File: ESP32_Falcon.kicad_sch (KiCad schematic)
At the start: 12 parts, among them J1 USB_C_Receptacle_USB2.0_16P, Q1 UMH3N, U1 ESP32-S3-WROOM-1, U2 USBLC6-2SC6, U3 AMS1117-3.3

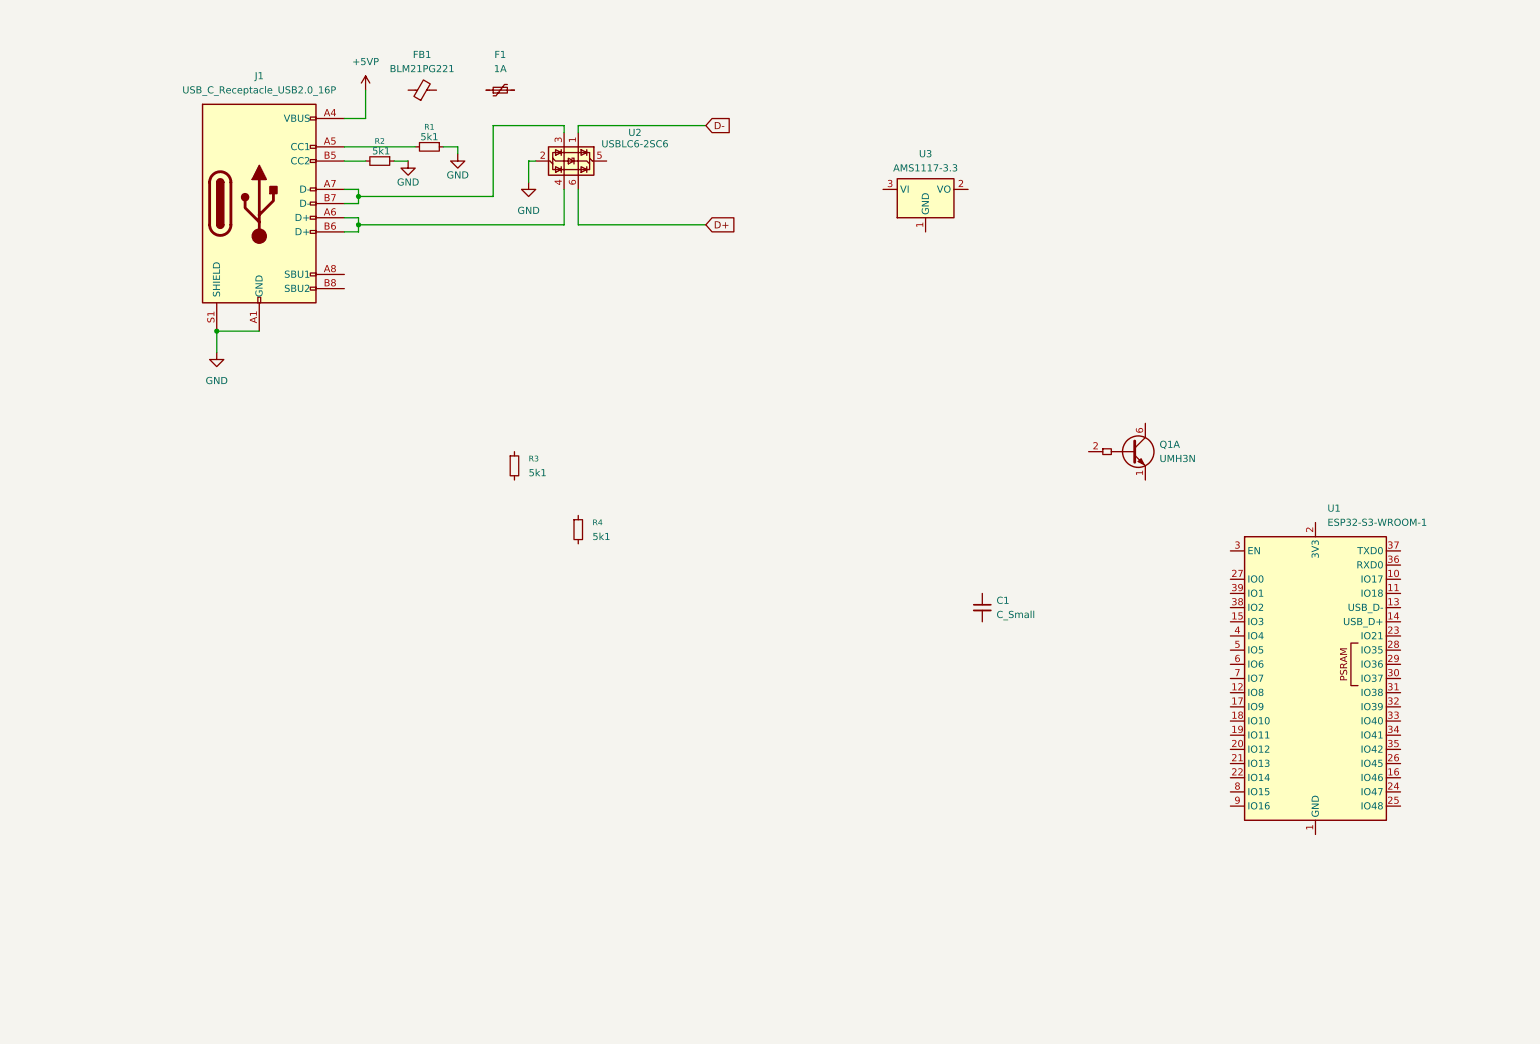
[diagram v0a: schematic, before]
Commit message: Praktycznie skonczony schematic
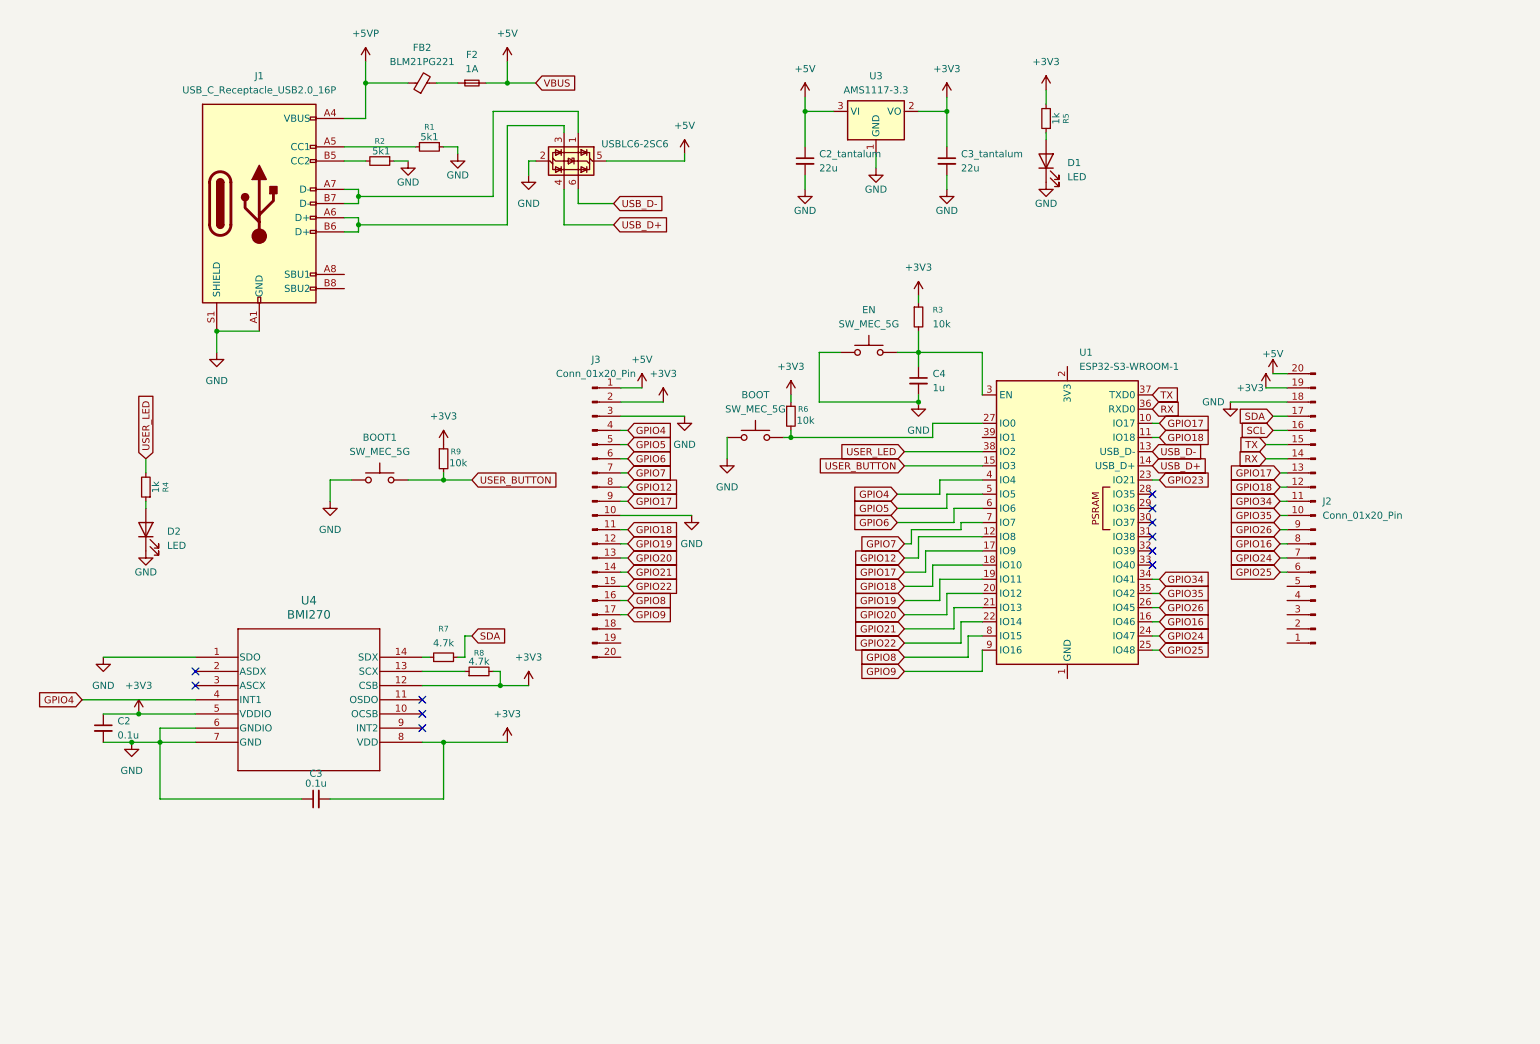
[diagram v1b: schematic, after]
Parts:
- removed C1: C_Small, Capacitor_SMD:C_0805_2012Metric_Pad1.18x1.45mm_HandSolder, symbol Device:C_Small
- removed F1: 1A, symbol Device:Polyfuse_Small
- removed FB1: BLM21PG221, symbol Device:FerriteBead_Small
- removed Q1: UMH3N, Package_TO_SOT_SMD:SOT-363_SC-70-6, symbol Transistor_BJT:UMH3N
- added BOOT, BOOT1: SW_MEC_5G, symbol Switch:SW_MEC_5G
- added C2, C3: 0.1u, Capacitor_SMD:C_0805_2012Metric_Pad1.18x1.45mm_HandSolder, symbol Device:C_Small
- added C2_tantalum, C3_tantalum: 22u, Capacitor_SMD:C_0805_2012Metric_Pad1.18x1.45mm_HandSolder, symbol Device:C_Small
- added C4: 1u, Capacitor_SMD:C_0805_2012Metric_Pad1.18x1.45mm_HandSolder, symbol Device:C_Small
- added D1, D2: LED, LED_SMD:LED_0805_2012Metric_Pad1.15x1.40mm_HandSolder, symbol Device:LED
- added EN: SW_MEC_5G, Button_Switch_SMD:SW_MEC_5GSH9, symbol Switch:SW_MEC_5G
- added F2: 1A, Fuse:Fuse_1206_3216Metric_Pad1.42x1.75mm_HandSolder, symbol Device:Fuse_Small
- added FB2: BLM21PG221, Inductor_SMD:L_0805_2012Metric_Pad1.05x1.20mm_HandSolder, symbol Device:FerriteBead_Small
- added J2, J3: Conn_01x20_Pin, Connector_PinHeader_2.54mm:PinHeader_1x20_P2.54mm_Vertical, symbol Connector:Conn_01x20_Pin
- added R5: 1k, Resistor_SMD:R_0805_2012Metric_Pad1.20x1.40mm_HandSolder, symbol Device:R_Small
- added R6, R9: 10k, Resistor_SMD:R_0805_2012Metric_Pad1.20x1.40mm_HandSolder, symbol Device:R_Small
- added R7, R8: 4.7k, Resistor_SMD:R_0805_2012Metric_Pad1.20x1.40mm_HandSolder, symbol Device:R_Small
- added U4: BMI270, BMI270_BOS, symbol 2026-03-31_17-21-26:BMI270
- R3: value 5k1 -> 10k
- R4: value 5k1 -> 1k
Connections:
- net D+ is gone; now on net USB_D-: U2.6 (I/O1)
- net D- is gone; now on an unnamed net: U2.1 (I/O1)
- net +5VP: now also FB2.1
- net GND: now also U3.1 (GND), BOOT.1 (A), BOOT.2 (A), BOOT1.1 (A), BOOT1.2 (A), C2.2, C2_tantalum.2, C3.1, C3_tantalum.2, C4.2, D1.1 (K), D2.1 (K), EN.1 (A), EN.2 (A), J2.18 (Pin_18), J3.10 (Pin_10), J3.3 (Pin_3), U4.1 (SDO), U4.6 (GNDIO), U4.7 (GND)
- net +3V3: now reaches U3.2 (VO)
- net +3V3: now also R3.1, C2.1, C3.2, C3_tantalum.1, J2.19 (Pin_19), J3.2 (Pin_2), R5.2, R6.1, R8.2, R9.1, U4.12 (CSB), U4.5 (VDDIO), U4.8 (VDD)
- net +5V: now reaches U3.3 (VI)
- net +5V: now also U2.5 (VBUS), C2_tantalum.1, F2.2, J2.20 (Pin_20), J3.1 (Pin_1)
- net GPIO17: now reaches U1.10 (IO17)
- net GPIO17: now also U1.17 (IO9), J2.13 (Pin_13), J3.9 (Pin_9)
- net GPIO18: now reaches U1.11 (IO18)
- net GPIO18: now also U1.18 (IO10), J2.12 (Pin_12), J3.11 (Pin_11)
- net GPIO12: now reaches U1.12 (IO8)
- net GPIO12: now also J3.8 (Pin_8)
- net USB_D-: now reaches U1.13 (USB_D-)
- net USB_D+: now reaches U1.14 (USB_D+)
- net USB_D+: now also U2.4 (I/O2)
- net USER_BUTTON: now reaches U1.15 (IO3)
- net USER_BUTTON: now also BOOT1.3 (B), BOOT1.4 (B), R9.2
- net GPIO16: now reaches U1.16 (IO46)
- net GPIO16: now also J2.8 (Pin_8)
- net GPIO19: now reaches U1.19 (IO11)
- net GPIO19: now also J3.12 (Pin_12)
- net GPIO20: now reaches U1.20 (IO12)
- net GPIO20: now also J3.13 (Pin_13)
- net GPIO21: now reaches U1.21 (IO13)
- net GPIO21: now also J3.14 (Pin_14)
- net GPIO22: now reaches U1.22 (IO14)
- net GPIO22: now also J3.15 (Pin_15)
- net GPIO23: now reaches U1.23 (IO21)
- net GPIO24: now reaches U1.24 (IO47)
- net GPIO24: now also J2.7 (Pin_7)
- net GPIO25: now reaches U1.25 (IO48)
- net GPIO25: now also J2.6 (Pin_6)
- net GPIO26: now reaches U1.26 (IO45)
- net GPIO26: now also J2.9 (Pin_9)
- net at U1.27 (IO0): now also BOOT.3 (B), BOOT.4 (B), R6.2
- net at U1.3 (EN): now also R3.2, C4.1, EN.3 (B), EN.4 (B)
- net GPIO34: now reaches U1.34 (IO41)
- net GPIO34: now also J2.11 (Pin_11)
- net GPIO35: now reaches U1.35 (IO42)
- net GPIO35: now also J2.10 (Pin_10)
- net RX: now reaches U1.36 (RXD0)
- net RX: now also J2.14 (Pin_14)
- net TX: now reaches U1.37 (TXD0)
- net TX: now also J2.15 (Pin_15)
- net USER_LED: now reaches U1.38 (IO2)
- net USER_LED: now also R4.2
- net GPIO4: now reaches U1.4 (IO4)
- net GPIO4: now also J3.4 (Pin_4), U4.4 (INT1)
- net GPIO5: now reaches U1.5 (IO5)
- net GPIO5: now also J3.5 (Pin_5)
- net GPIO6: now reaches U1.6 (IO6)
- net GPIO6: now also J3.6 (Pin_6)
- net GPIO7: now reaches U1.7 (IO7)
- net GPIO7: now also J3.7 (Pin_7)
- net GPIO8: now reaches U1.8 (IO15)
- net GPIO8: now also J3.16 (Pin_16)
- net GPIO9: now reaches U1.9 (IO16)
- net GPIO9: now also J3.17 (Pin_17)
- net at J1.A7 (D-), J1.B7 (D-): no longer U2.3 (I/O2)
- net at J1.A6 (D+), J1.B6 (D+): now also U2.3 (I/O2); no longer U2.4 (I/O2)
- net at R4.1: now also D2.2 (A)
- new net: R8.1, U4.13 (SCX)
- new net: R7.1, U4.14 (SDX)
- new net: F2.1, FB2.2
- new net: D1.2 (A), R5.1
- new net SCL: J2.16 (Pin_16)
- new net SDA: J2.17 (Pin_17), R7.2
- no-connect marks 0 -> 11
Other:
- moved on the sheet: R3, U1, U3

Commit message: Poczatek PCB
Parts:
- removed BOOT, BOOT1: SW_MEC_5G, symbol Switch:SW_MEC_5G
- removed EN: SW_MEC_5G, Button_Switch_SMD:SW_MEC_5GSH9, symbol Switch:SW_MEC_5G
- added BOOT1, EN1, USER_BUTTON1: SW_Push, Button_Switch_SMD:SW_Push_1TS009xxxx-xxxx-xxxx_6x6x5mm, symbol Switch:SW_Push
- J1: footprint (none) -> Connector_USB:USB_C_Receptacle_XKB_U262-16XN-4BVC11
- U4: footprint BMI270_BOS -> footprints:BMI270_BOS
- renumbered C2_tantalum to C2_tantalum1, C3_tantalum to C3_tantalum1
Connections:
- net +3V3: now also U1.2 (3V3)
- net GND: now also U1.1 (GND), U1.40 (GND), U1.41 (GND), BOOT1.1, EN1.1, USER_BUTTON1.1
- net GPIO17: no longer J2.13 (Pin_13), U1.10 (IO17)
- net GPIO18: no longer J2.12 (Pin_12), U1.11 (IO18)
- net GPIO19: no longer U1.19 (IO11)
- net GPIO20: no longer U1.20 (IO12)
- net USER_BUTTON: now also USER_BUTTON1.2
- net at R6.2, U1.27 (IO0): now also BOOT1.2
- net at C4.1, R3.2, U1.3 (EN): now also EN1.2
- new net GPIO10: J2.13 (Pin_13), U1.10 (IO17)
- new net GPIO11: J2.12 (Pin_12), U1.11 (IO18)
- no-connect marks 11 -> 21
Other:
- note added: "BMI 270"
- note added: "MCU"
- note added: "POWER INTERFACE"
- note added: "USER BUTTON"
- note added: "USER LED"
- moved on the sheet: C2, C3, C4, D2, J2, J3, R3, R4, R6, R7, R8, R9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

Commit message: skończony projekt
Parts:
- removed J2, J3: Conn_01x20_Pin, Connector_PinHeader_2.54mm:PinHeader_1x20_P2.54mm_Vertical, symbol Connector:Conn_01x20_Pin
- added J2, J3: Conn_01x15_Pin, Connector_PinHeader_2.54mm:PinHeader_1x15_P2.54mm_Vertical, symbol Connector:Conn_01x15_Pin
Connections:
- net GPIO8 is gone; now on net SDA: U1.8 (IO15)
- net GPIO9 is gone; now on net SCL: U1.9 (IO16)
- net +3V3: now also J2.2 (Pin_2), J3.14 (Pin_14); no longer R8.2
- net +5V: now also J2.1 (Pin_1), J3.15 (Pin_15)
- net GND: now also J2.10 (Pin_10), J2.3 (Pin_3), J3.13 (Pin_13)
- net GPIO10: now also J3.8 (Pin_8)
- net GPIO11: now also J3.7 (Pin_7)
- net GPIO12: now also J2.8 (Pin_8)
- net GPIO16: now also J3.3 (Pin_3)
- net GPIO17: now also J2.9 (Pin_9)
- net GPIO18: now also J2.11 (Pin_11)
- net GPIO21: now also J2.15 (Pin_15)
- net GPIO22: now also J2.14 (Pin_14)
- net GPIO23: now also J2.13 (Pin_13)
- net GPIO24: now also J3.2 (Pin_2)
- net GPIO25: now also J3.1 (Pin_1)
- net GPIO26: now also J3.4 (Pin_4)
- net GPIO34: now also J3.6 (Pin_6)
- net GPIO35: now also J3.5 (Pin_5)
- net GPIO4: now also J2.4 (Pin_4)
- net GPIO5: now also J2.5 (Pin_5)
- net GPIO6: now also J2.6 (Pin_6)
- net GPIO7: now also J2.7 (Pin_7)
- net RX: now also J3.10 (Pin_10)
- net SCL: now also R8.2, J3.11 (Pin_11)
- net SDA: now also J3.12 (Pin_12)
- net TX: now also J3.9 (Pin_9)
- no-connect marks 21 -> 14
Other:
- moved on the sheet: R7, R8
